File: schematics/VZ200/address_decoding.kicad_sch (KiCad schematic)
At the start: 34 parts, among them J901 Cassette, J903 Keyboard, Q900 9018, U1 74LS174, U12 74LS244, U2 74LS32, U3 74LS139

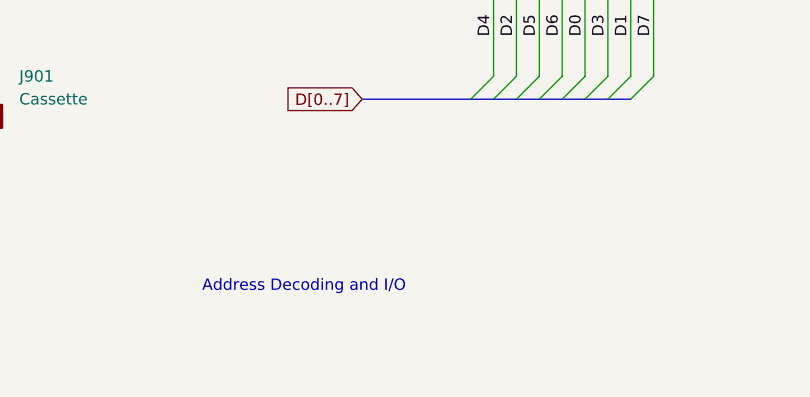
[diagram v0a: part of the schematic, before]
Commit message: Schematic for the VZ200 printer interface
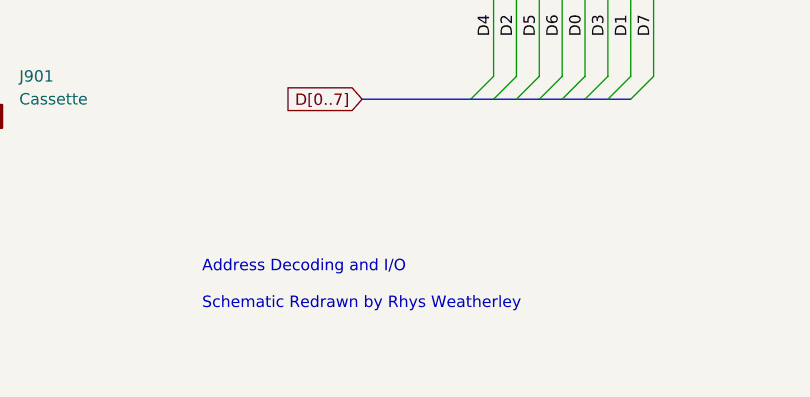
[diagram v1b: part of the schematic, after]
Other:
- note added: "Address Decoding and I/O Schematic Redrawn by Rhys Weatherley"
- note removed: "Address Decoding and I/O"
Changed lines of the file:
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@@
     (effects (font (size 1.27 1.27)) (justify left bottom))
   )
-  (text "Address Decoding and I/O" (at 182.245 174.625 0)
+  (text "Address Decoding and I/O\n\nSchematic Redrawn by Rhys Weatherley"
+    (at 182.245 176.53 0)
     (effects (font (size 1.27 1.27)) (justify left bottom))
   )

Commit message: Add title and revision details to the schematic sheets
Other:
- title: (none) -> VZ200 Computer
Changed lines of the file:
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@@
 (kicad_sch (version 20230121) (generator eeschema)
   (paper "A4")
+  (title_block
+    (title "VZ200 Computer")
+    (date "2024-01-01")
+    (rev "1")
+  )
   (junction (at 116.205 61.595) (diameter 0) (color 0 0 0 0)
   )

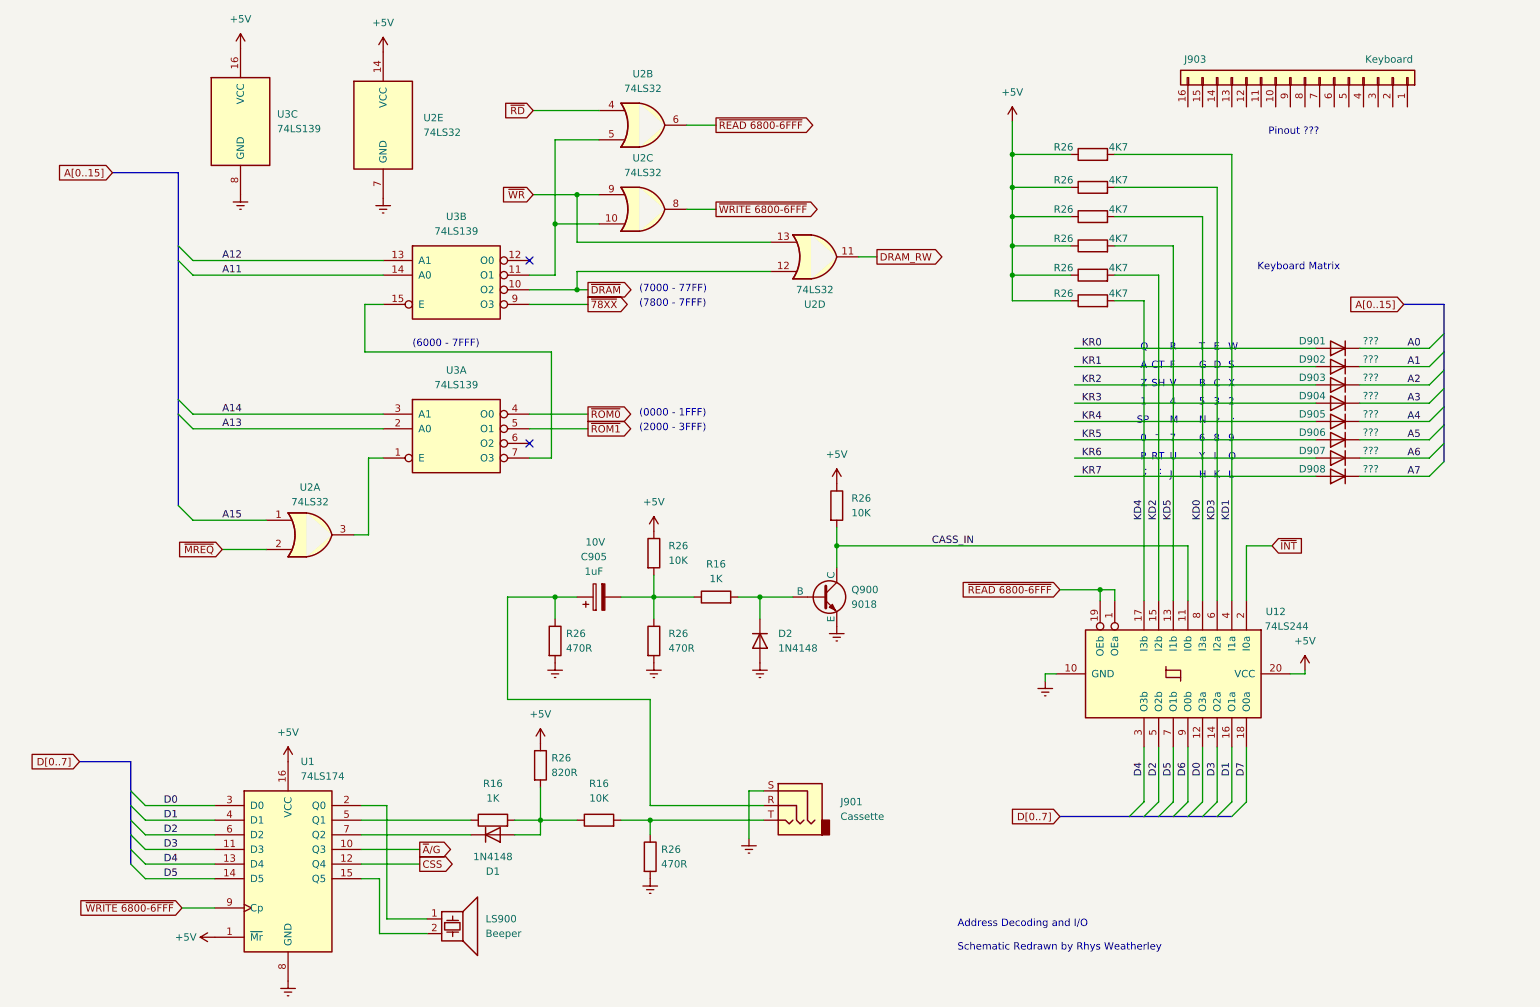
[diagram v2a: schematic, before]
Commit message: Update motherboard schematic based on inspection of the actual board
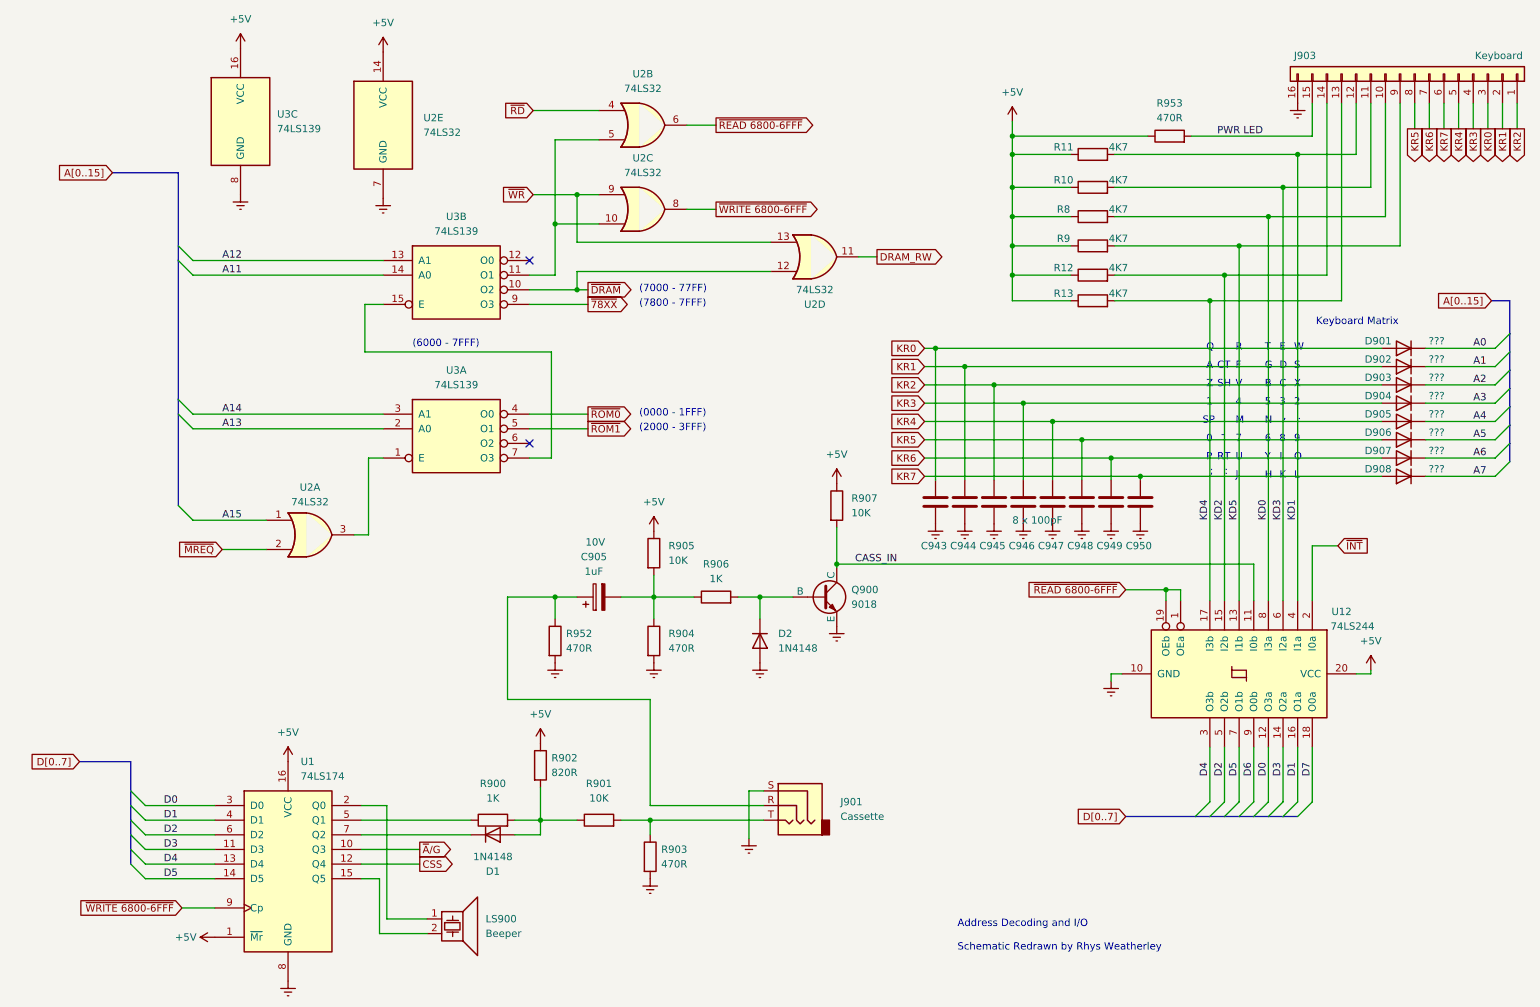
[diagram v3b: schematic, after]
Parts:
- added C943: 8 x 100pF, Capacitor_THT:C_Disc_D5.0mm_W2.5mm_P5.00mm, symbol Device:C
- added C944, C945, C946, C947, C948, C949, C950: 100pF, Capacitor_THT:C_Disc_D5.0mm_W2.5mm_P5.00mm, symbol Device:C
- added R953: 470R, Resistor_THT:R_Axial_DIN0207_L6.3mm_D2.5mm_P7.62mm_Horizontal, symbol Device:R
- renumbered R26 to R10, R26 to R11, R26 to R12, R26 to R13, R26 to R8, R26 to R9, R16 to R900, R16 to R901, R26 to R902, R26 to R903, R26 to R904, R26 to R905, R16 to R906, R26 to R907, R26 to R952
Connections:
- net +5V: now also R953.1
- net Earth: now also J903.16 (Pin_16), C943.2, C944.2, C945.2, C946.2, C947.2, C948.2, C949.2, C950.2
- net KD0: now also J903.10 (Pin_10)
- net KD1: now also J903.12 (Pin_12)
- net KD2: now also J903.14 (Pin_14)
- net KD3: now also J903.11 (Pin_11)
- net KD4: now also J903.13 (Pin_13)
- net KD5: now also J903.9 (Pin_9)
- net KR0: now also J903.3 (Pin_3), C943.1
- net KR1: now also J903.2 (Pin_2), C944.1
- net KR2: now also J903.1 (Pin_1), C945.1
- net KR3: now also J903.4 (Pin_4), C946.1
- net KR4: now also J903.5 (Pin_5), C947.1
- net KR5: now also J903.8 (Pin_8), C948.1
- net KR6: now also J903.7 (Pin_7), C949.1
- net KR7: now also J903.6 (Pin_6), C950.1
- net PWR LED: now reaches J903.15 (Pin_15)
- net PWR LED: now also R953.2
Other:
- note removed: "Pinout ???"
- moved on the sheet: D901, D902, D903, D904, D905, D906, D907, D908, J903, U12

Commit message: Restoration Part 2
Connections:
- net at C905.1, R952.1: now also J901.T; no longer J901.R
- net at R901.2, R903.1: now also J901.R; no longer J901.T
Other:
- moved on the sheet: J901
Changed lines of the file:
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@@
   (junction (at 112.395 50.165) (diameter 0) (color 0 0 0 0)
   )
+  (junction (at 128.905 153.67) (diameter 0) (color 0 0 0 0)
+  )
   (junction (at 178.435 71.755) (diameter 0) (color 0 0 0 0)
   )
@@
   (junction (at 198.755 84.455) (diameter 0) (color 0 0 0 0)
   )
-  (junction (at 128.905 153.67) (diameter 0) (color 0 0 0 0)
-  )
   (junction (at 112.395 114.935) (diameter 0) (color 0 0 0 0)
   )
@@
     (stroke (width 0) (type default))
   )
-  (wire (pts (xy 148.59 148.59) (xy 146.05 148.59))
-    (stroke (width 0) (type default))
-  )
   (bus (pts (xy 228.6 153.035) (xy 231.14 153.035))
     (stroke (width 0) (type default))
@@
     (stroke (width 0) (type default))
   )
-  (wire (pts (xy 148.59 151.13) (xy 128.905 151.13))
+  (wire (pts (xy 104.14 132.715) (xy 104.14 114.935))
     (stroke (width 0) (type default))
   )
-  (wire (pts (xy 104.14 132.715) (xy 104.14 114.935))
+  (wire (pts (xy 148.59 156.21) (xy 143.51 156.21))
     (stroke (width 0) (type default))
   )
@@
     (stroke (width 0) (type default))
   )
+  (wire (pts (xy 128.905 153.67) (xy 148.59 153.67))
+    (stroke (width 0) (type default))
+  )
   (bus (pts (xy 278.13 88.265) (xy 278.13 85.09))
     (stroke (width 0) (type default))
@@
     (stroke (width 0) (type default))
   )
-  (wire (pts (xy 146.05 148.59) (xy 146.05 156.845))
-    (stroke (width 0) (type default))
-  )
-  (wire (pts (xy 128.905 153.67) (xy 148.59 153.67))
+  (wire (pts (xy 146.05 151.13) (xy 146.05 159.385))
     (stroke (width 0) (type default))
   )
@@
     (stroke (width 0) (type default))
   )
+  (wire (pts (xy 146.05 151.13) (xy 148.59 151.13))
+    (stroke (width 0) (type default))
+  )
   (wire (pts (xy 116.205 53.34) (xy 149.86 53.34))
     (stroke (width 0) (type default))
@@
     (stroke (width 0) (type default))
   )
-  (wire (pts (xy 128.905 151.13) (xy 128.905 132.715))
+  (wire (pts (xy 143.51 132.715) (xy 143.51 156.21))
     (stroke (width 0) (type default))
   )
@@
     (stroke (width 0) (type default))
   )
-  (wire (pts (xy 128.905 132.715) (xy 104.14 132.715))
+  (wire (pts (xy 143.51 132.715) (xy 104.14 132.715))
     (stroke (width 0) (type default))
   )
@@
     )
   )
-  (symbol (lib_id "power:Earth") (at 146.05 156.845 0) (unit 1)
+  (symbol (lib_id "power:Earth") (at 146.05 159.385 0) (unit 1)
     (in_bom yes) (on_board yes) (dnp no) (fields_autoplaced)
-    (property "Reference" "#PWR039" (at 146.05 163.195 0)
+    (property "Reference" "#PWR039" (at 146.05 165.735 0)
       (effects (font (size 1.27 1.27)) hide)
     )
-    (property "Value" "Earth" (at 146.05 160.655 0)
+    (property "Value" "Earth" (at 146.05 163.195 0)
       (effects (font (size 1.27 1.27)) hide)
     )
-    (property "Footprint" "" (at 146.05 156.845 0)
+    (property "Footprint" "" (at 146.05 159.385 0)
       (effects (font (size 1.27 1.27)) hide)
     )
-    (property "Datasheet" "~" (at 146.05 156.845 0)
+    (property "Datasheet" "~" (at 146.05 159.385 0)
       (effects (font (size 1.27 1.27)) hide)
     )
@@
     )
   )
-  (symbol (lib_id "Connector_Audio:AudioJack3") (at 153.67 151.13 0) (mirror y) (unit 1)
+  (symbol (lib_id "Connector_Audio:AudioJack3") (at 153.67 153.67 0) (mirror y) (unit 1)
     (in_bom yes) (on_board yes) (dnp no) (fields_autoplaced)
-    (property "Reference" "J901" (at 161.925 150.495 0)
+    (property "Reference" "J901" (at 161.925 153.035 0)
       (effects (font (size 1.27 1.27)) (justify right))
     )
-    (property "Value" "Cassette" (at 161.925 153.035 0)
+    (property "Value" "Cassette" (at 161.925 155.575 0)
       (effects (font (size 1.27 1.27)) (justify right))
     )
-    (property "Footprint" "" (at 153.67 151.13 0)
+    (property "Footprint" "" (at 153.67 153.67 0)
       (effects (font (size 1.27 1.27)) hide)
     )
-    (property "Datasheet" "~" (at 153.67 151.13 0)
+    (property "Datasheet" "~" (at 153.67 153.67 0)
       (effects (font (size 1.27 1.27)) hide)
     )
